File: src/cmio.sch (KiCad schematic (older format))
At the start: 35 parts, among them J1 USB_POWER, J3 BANK0, J4 USB_OTG, J5 CM3Lite, J6 TVOUT, J7 BANK1, J8 Micro_SD_Card_TFP09_2_12B, SW1 Reset, U1 AP3417B, U2 AP3417B, U3 SP6203EM5-L-2-8/TR, U4 AP2401

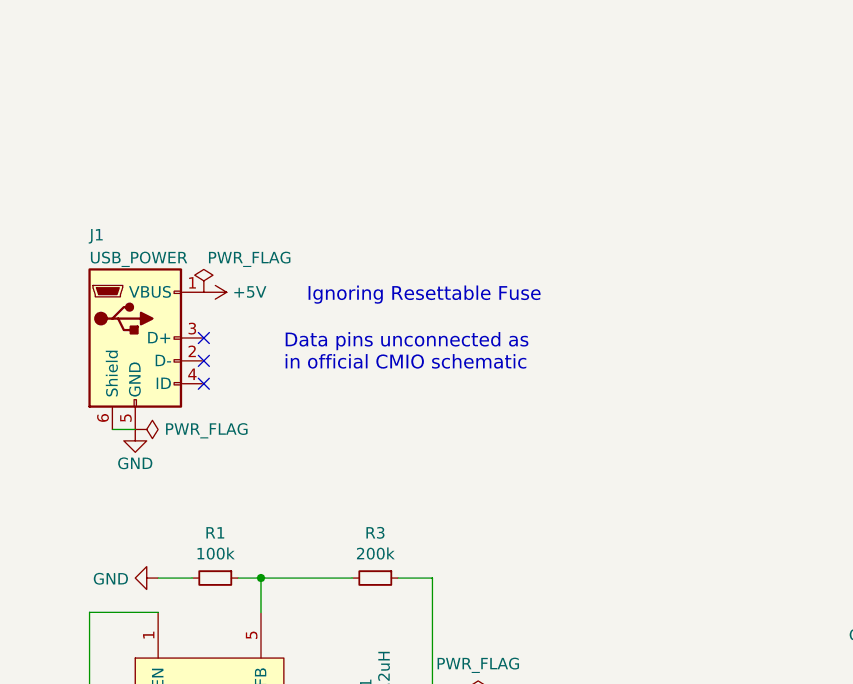
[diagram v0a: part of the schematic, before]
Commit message: Add test points
Signed-off-by: Mahyar Koshkouei <mahyar.koshkouei@gmail.com>
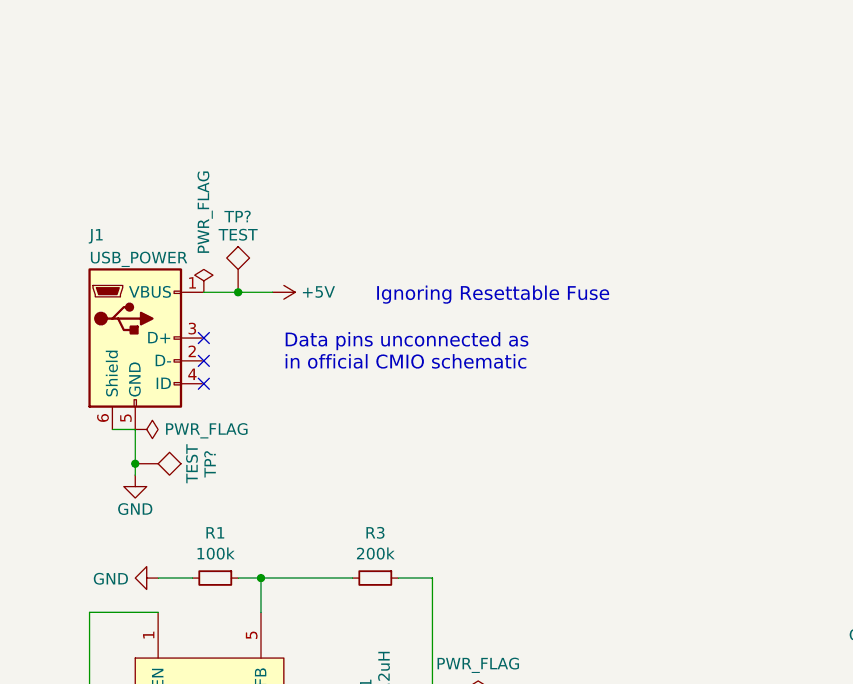
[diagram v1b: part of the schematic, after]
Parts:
- added TP? (x2): TEST, symbol TEST
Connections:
- net +5V: now also TP?.1
- net GND: now also TP?.1
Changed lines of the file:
@@
 L +5V #PWR08
 U 1 1 5925EDB5
-P 1550 3750
-F 0 "#PWR08" H 1550 3600 50  0001 C CNN
-F 1 "+5V" V 1550 3950 50  0000 C CNN
-F 2 "" H 1550 3750 50  0001 C CNN
-F 3 "" H 1550 3750 50  0001 C CNN
-	1    1550 3750
+P 1850 3750
+F 0 "#PWR08" H 1850 3600 50  0001 C CNN
+F 1 "+5V" V 1850 3950 50  0000 C CNN
+F 2 "" H 1850 3750 50  0001 C CNN
+F 3 "" H 1850 3750 50  0001 C CNN
+	1    1850 3750
 	0    1    1    0
 $EndComp
@@
 L GND #PWR029
 U 1 1 5925E739
-P 1250 4350
-F 0 "#PWR029" H 1250 4100 50  0001 C CNN
-F 1 "GND" H 1250 4200 50  0000 C CNN
-F 2 "" H 1250 4350 50  0001 C CNN
-F 3 "" H 1250 4350 50  0001 C CNN
-	1    1250 4350
+P 1250 4550
+F 0 "#PWR029" H 1250 4300 50  0001 C CNN
+F 1 "GND" H 1250 4400 50  0000 C CNN
+F 2 "" H 1250 4550 50  0001 C CNN
+F 3 "" H 1250 4550 50  0001 C CNN
+	1    1250 4550
 	1    0    0    -1
 $EndComp
@@
 P 1550 3750
 F 0 "#FLG031" H 1550 3825 50  0001 C CNN
-F 1 "PWR_FLAG" H 1750 3900 50  0000 C CNN
+F 1 "PWR_FLAG" V 1550 4100 50  0000 C CNN
 F 2 "" H 1550 3750 50  0001 C CNN
 F 3 "" H 1550 3750 50  0001 C CNN
@@
 $EndComp
 NoConn ~ 8650 7650
-Text Notes 2000 3800 0    60   ~ 0
+Text Notes 2300 3800 0    60   ~ 0
 Ignoring Resettable Fuse
 Text Notes 1900 4100 0    60   ~ 0
@@
 Text Label 5950 3100 2    60   ~ 0
 BCM_27
+$Comp
+L CP1_Small C12
+U 1 1 59C026E4
+P 4450 5550
+F 0 "C12" H 4541 5596 50  0000 L CNN
+F 1 "47uF" H 4541 5505 50  0000 L CNN
+F 2 "Capacitors_Tantalum_SMD:CP_Tantalum_Case-A_EIA-3216-18_Hand" H 4450 5550 50  0001 C CNN
+F 3 "" H 4450 5550 50  0001 C CNN
+	1    4450 5550
+	-1   0    0    1
+$EndComp
+$Comp
+L GND #PWR052
+U 1 1 59C026EA
+P 4450 5400
+F 0 "#PWR052" H 4450 5150 50  0001 C CNN
+F 1 "GND" H 4450 5250 50  0000 C CNN
+F 2 "" H 4450 5400 50  0001 C CNN
+F 3 "" H 4450 5400 50  0001 C CNN
+	1    4450 5400
+	-1   0    0    1
+$EndComp
+$Comp
+L TEST TP?
+U 1 1 59C4E52B
+P 1700 3750
+F 0 "TP?" H 1700 4050 50  0000 C BNN
+F 1 "TEST" H 1700 4000 50  0000 C CNN
+F 2 "" H 1700 3750 50  0001 C CNN
+F 3 "" H 1700 3750 50  0001 C CNN
+	1    1700 3750
+	1    0    0    -1
+$EndComp
+$Comp
+L TEST TP?
+U 1 1 59C4E7A6
+P 1250 4500
+F 0 "TP?" H 1250 4800 50  0000 C BNN
+F 1 "TEST" H 1250 4750 50  0000 C CNN
+F 2 "" H 1250 4500 50  0001 C CNN
+F 3 "" H 1250 4500 50  0001 C CNN
+	1    1250 4500
+	0    1    1    0
+$EndComp
 Wire Wire Line
 	6300 6750 6750 6750
@@
 Wire Bus Line
 	6050 1300 6100 1300
-$Comp
-L CP1_Small C12
-U 1 1 59C026E4
-P 4450 5550
-F 0 "C12" H 4541 5596 50  0000 L CNN
-F 1 "47uF" H 4541 5505 50  0000 L CNN
-F 2 "Capacitors_Tantalum_SMD:CP_Tantalum_Case-A_EIA-3216-18_Hand" H 4450 5550 50  0001 C CNN
-F 3 "" H 4450 5550 50  0001 C CNN
-	1    4450 5550
-	-1   0    0    1
-$EndComp
-$Comp
-L GND #PWR052
-U 1 1 59C026EA
-P 4450 5400
-F 0 "#PWR052" H 4450 5150 50  0001 C CNN
-F 1 "GND" H 4450 5250 50  0000 C CNN
-F 2 "" H 4450 5400 50  0001 C CNN
-F 3 "" H 4450 5400 50  0001 C CNN
-	1    4450 5400
-	-1   0    0    1
-$EndComp
 Wire Wire Line
 	4450 5450 4450 5400
@@
 	3950 5650 4650 5650
 Connection ~ 4450 5650
+Wire Wire Line
+	1250 4350 1250 4550
+Connection ~ 1250 4500
+Wire Wire Line
+	1550 3750 1850 3750
+Connection ~ 1700 3750
 $EndSCHEMATC

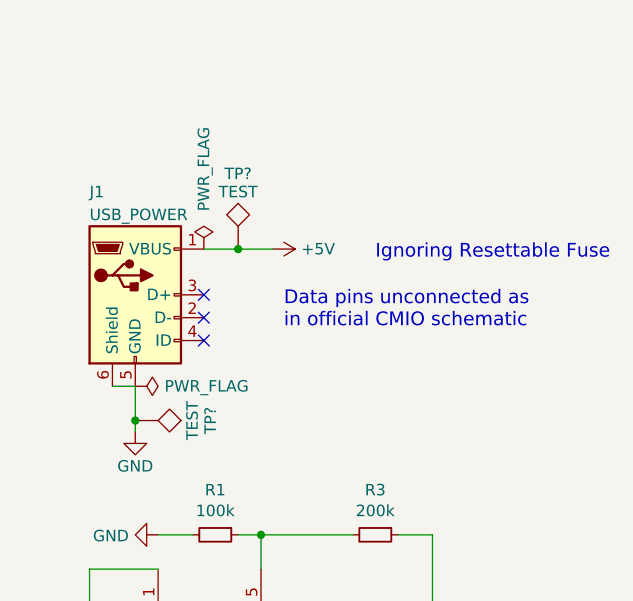
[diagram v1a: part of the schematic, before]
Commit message: Change Micro USB footprint with circular pads only
For support with OSH Park.

Signed-off-by: Mahyar Koshkouei <mahyar.koshkouei@gmail.com>
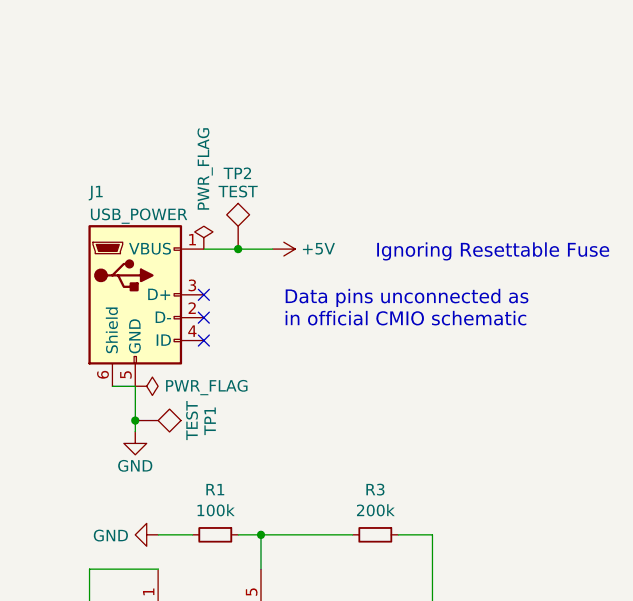
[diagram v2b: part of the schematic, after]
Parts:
- TP1, TP2: renamed from TP?; footprint (none) -> Measurement_Points:Measurement_Point_Round-SMD-Pad_Small
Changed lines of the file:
@@
 Sheet 1 1
 Title "Custom Compute Module IO Board"
-Date "2017-09-19"
+Date "2017-09-22"
 Rev ""
 Comp "Mahyar Koshkouei"
@@
 $EndComp
 $Comp
-L TEST TP?
+L TEST TP2
 U 1 1 59C4E52B
 P 1700 3750
-F 0 "TP?" H 1700 4050 50  0000 C BNN
+F 0 "TP2" H 1700 4050 50  0000 C BNN
 F 1 "TEST" H 1700 4000 50  0000 C CNN
-F 2 "" H 1700 3750 50  0001 C CNN
+F 2 "Measurement_Points:Measurement_Point_Round-SMD-Pad_Small" H 1700 3750 50  0001 C CNN
 F 3 "" H 1700 3750 50  0001 C CNN
 	1    1700 3750
@@
 $EndComp
 $Comp
-L TEST TP?
+L TEST TP1
 U 1 1 59C4E7A6
 P 1250 4500
-F 0 "TP?" H 1250 4800 50  0000 C BNN
+F 0 "TP1" H 1250 4800 50  0000 C BNN
 F 1 "TEST" H 1250 4750 50  0000 C CNN
-F 2 "" H 1250 4500 50  0001 C CNN
+F 2 "Measurement_Points:Measurement_Point_Round-SMD-Pad_Small" H 1250 4500 50  0001 C CNN
 F 3 "" H 1250 4500 50  0001 C CNN
 	1    1250 4500

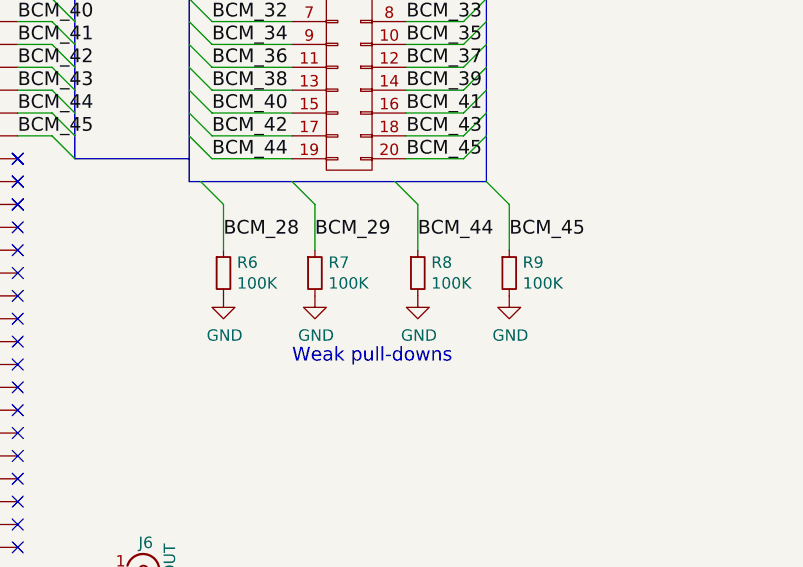
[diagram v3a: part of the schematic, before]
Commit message: Use little k for resistor values
Signed-off-by: Mahyar Koshkouei <mahyar.koshkouei@gmail.com>
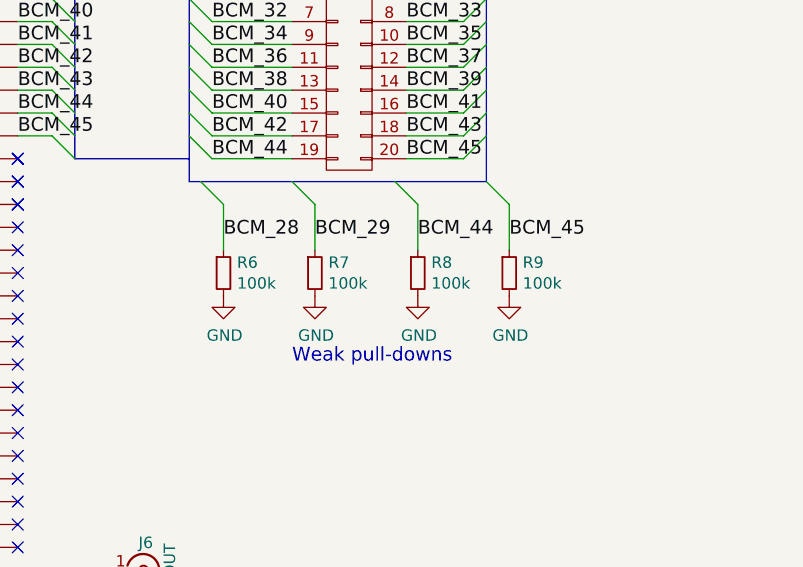
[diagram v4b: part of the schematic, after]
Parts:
- R6, R7, R8, R9: value 100K -> 100k
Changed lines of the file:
@@
 P 11450 4450
 F 0 "R6" H 11509 4496 50  0000 L CNN
-F 1 "100K" H 11509 4405 50  0000 L CNN
+F 1 "100k" H 11509 4405 50  0000 L CNN
 F 2 "Resistors_SMD:R_0805_HandSoldering" H 11450 4450 50  0001 C CNN
 F 3 "" H 11450 4450 50  0001 C CNN
@@
 P 11850 4450
 F 0 "R7" H 11909 4496 50  0000 L CNN
-F 1 "100K" H 11909 4405 50  0000 L CNN
+F 1 "100k" H 11909 4405 50  0000 L CNN
 F 2 "Resistors_SMD:R_0805_HandSoldering" H 11850 4450 50  0001 C CNN
 F 3 "" H 11850 4450 50  0001 C CNN
@@
 P 12300 4450
 F 0 "R8" H 12359 4496 50  0000 L CNN
-F 1 "100K" H 12359 4405 50  0000 L CNN
+F 1 "100k" H 12359 4405 50  0000 L CNN
 F 2 "Resistors_SMD:R_0805_HandSoldering" H 12300 4450 50  0001 C CNN
 F 3 "" H 12300 4450 50  0001 C CNN
@@
 P 12700 4450
 F 0 "R9" H 12759 4496 50  0000 L CNN
-F 1 "100K" H 12759 4405 50  0000 L CNN
+F 1 "100k" H 12759 4405 50  0000 L CNN
 F 2 "Resistors_SMD:R_0805_HandSoldering" H 12700 4450 50  0001 C CNN
 F 3 "" H 12700 4450 50  0001 C CNN

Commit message: Major Changes
- Add USB Boot setting
- Add Status and Power LEDs
- Added a second Micro SD slot with a different footprint to allow users
more variety. They cannot be used at the same time.
- Use 2.5V for Video DAC, as used in the official CMIO board.
- Add test points.
- Change decoupling capacitor at Micro SD card slot.
- Change tantalum capacitor footprints at USB port to non-handsoldering.
The handsoldering footprint uses larger than required pads when using a
heat gun.

Signed-off-by: Mahyar Koshkouei <mahyar.koshkouei@gmail.com>
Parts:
- removed C5: 10nF, Capacitors_SMD:C_0805_HandSoldering, symbol C_Small
- removed J7: BANK1, Pin_Headers:Pin_Header_Straight_2x10_Pitch2.54mm_SMD, symbol CONN_02X10
- removed U3: SP6203EM5-L-2-8/TR, TO_SOT_Packages_SMD:SOT-23-5_HandSoldering, symbol SP6203
- added D1: PWR LED, LEDs:LED_0805, symbol LED
- added D2: STATUS LED, LEDs:LED_0805, symbol LED
- added J9: Micro_SD_Card_Molex_47219-2001, foot:Molex_Micro_SD_47309-3751, symbol Micro_SD_Card_Molex_47219-2001
- added J?: Conn_02x11_Odd_Even, symbol Conn_02x11_Odd_Even
- added Q1, Q2: 2N7002, TO_SOT_Packages_SMD:SOT-23, symbol MMBF170
- added R11, R12: 100K, Resistors_SMD:R_0805_HandSoldering, symbol R_Small
- added R13, R5: 470, Resistors_SMD:R_0805_HandSoldering, symbol R_Small
- added TP3, TP4: TEST, Measurement_Points:Measurement_Point_Round-SMD-Pad_Small, symbol TEST
- added U3: AP2138, TO_SOT_Packages_SMD:SOT-23, symbol AP2138
- C10: footprint Capacitors_Tantalum_SMD:CP_Tantalum_Case-A_EIA-3216-18_Hand -> Capacitors_Tantalum_SMD:CP_Tantalum_Case-A_EIA-3216-18_Reflow
- C11: value 0.1uF -> 4.7uF
- C3, C4: value 4.7uF -> 1uF
- C7: renamed from C12; footprint Capacitors_Tantalum_SMD:CP_Tantalum_Case-A_EIA-3216-18_Hand -> Capacitors_Tantalum_SMD:CP_Tantalum_Case-A_EIA-3216-18_Reflow
- J1: footprint foot:Molex_Right_Angle_SMT_TypeB_MicroUSB_105017 -> foot:Molex_Right_Angle_SMT_TypeB_MicroUSB_105017_CircularOnly_annular_fix
- J3: renamed from J4; footprint foot:Molex_Right_Angle_SMT_TypeB_MicroUSB_105017 -> foot:Molex_Right_Angle_SMT_TypeB_MicroUSB_105017_CircularOnly_annular_fix
- J4: renamed from J5; footprint foot:CM3_Socket_SODIMM_DDR1-2_TE_1612618_NoHole -> foot:CM3_Socket_SODIMM_DDR1-2_TE_1473149_4_NoHole_NoEndSilkS
- renumbered C6 to C5, C7 to C6, J3 to J2, J6 to J5, J8 to J7, R9 to R10, R5 to R6, R6 to R7, R7 to R8, R8 to R9
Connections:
- net +1V8: now also R12.1
- net +3V3: now also D1.2 (A), D2.2 (A), J9.4 (VDD), J?.1 (Pin_1)
- net +5V: now also U3.3 (VIN)
- net BCM_28: now also J?.3 (Pin_3)
- net BCM_29: now also J?.4 (Pin_4)
- net BCM_30: now also J?.5 (Pin_5)
- net BCM_31: now also J?.6 (Pin_6)
- net BCM_32: now also J?.7 (Pin_7)
- net BCM_33: now also J?.8 (Pin_8)
- net BCM_34: now also J?.9 (Pin_9)
- net BCM_35: now also J?.10 (Pin_10)
- net BCM_36: now also J?.11 (Pin_11)
- net BCM_37: now also J?.12 (Pin_12)
- net BCM_38: now also J?.13 (Pin_13)
- net BCM_39: now also J?.14 (Pin_14)
- net BCM_40: now also J?.15 (Pin_15)
- net BCM_41: now also J?.16 (Pin_16)
- net BCM_42: now also J?.17 (Pin_17)
- net BCM_43: now also J?.18 (Pin_18)
- net BCM_44: now also J?.19 (Pin_19)
- net BCM_45: now also J?.20 (Pin_20)
- net CLK: now also J9.5 (CLK)
- net CMD: now also J9.3 (CMD)
- net DAT0: now also J9.7 (DAT0)
- net DAT1: now also J9.8 (DAT1)
- net DAT2: now also J9.1 (DAT2)
- net DAT3: now also J9.2 (DAT3/CD)
- net GND: now also J9.10 (G2), J9.6 (VSS), J9.9 (G1), J?.2 (Pin_2), Q2.2 (S), R11.2, R5.2, U3.1 (GND)
- net TV: now reaches J4.166 (TVDAC), J5.1 (In)
- net RESET: now reaches J4.177 (RUN), SW1.2
- net EMMC_DISABLE_N: now reaches J4.2 (EMMC_DISABLE_N)
- net EMMC_DISABLE_N: now also Q1.3 (D), TP3.1
- net STATUS_LED: now reaches J4.90 (EMMC_EN_N_1V8)
- net STATUS_LED: now also Q2.1 (G), R12.2, TP4.1
- net VBUS: now reaches C10.1, C9.1, J3.1 (VBUS), U4.6 (OUT), U4.7 (OUT), U4.8 (NC)
- net VBUS: now also J?.21 (Pin_21)
- net +2V8 renamed +2V5
- net +2V5: now also U3.2 (VOUT)
- new net: D2.1 (K), R13.1
- new net: Q1.2 (S), Q2.3 (D), R13.2
- new net: D1.1 (K), R5.1
- new net USB_SET: J?.22 (Pin_22), Q1.1 (G), R11.1
- no-connect marks 59 -> 56
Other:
- note added: "USB OTG Power Switch IC"
- note added: "VBUS-USB_SET Jumper Setting:\n CONNECTED = USB BOOT ENABLED\n NOT CONNECTED = USB BOOT DISABLED"
- note removed: "Expecting maximum temperature of 36C\n(Vo=2.8, Vin=5, Ta=25C)"
- moved on the sheet: C10, C3, C4, C7, C8, C9, J1, J3, J7, R10, R6, R7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
